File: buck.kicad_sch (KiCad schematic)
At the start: 0 parts

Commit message: Added Symbols and Buck Converter
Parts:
- added C1: 0.1uFCap, CAPC2012X94N, symbol group127:0.1uFCap
- added C2: 0.1uF, CAPC2012X94N, symbol group127:0.1uFCap
- added C3, C4: 22uF, CAPC2012X94N, symbol group127:0.1uFCap
- added L1: 6.8uH, 7447707068, symbol group127:Inductor
- added R1: 100k, RESC2012X60N, symbol group127:Resistor
- added R2: 13.7k, RESC2012X60N, symbol group127:Resistor
- added U1: LMR51430, Package_TO_SOT_SMD:SOT-23-6, symbol Regulator_Switching:LMR51430
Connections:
- new net: R1.1, R2.1, U1.4 (FB)
- new net: C3.1, C4.1, L1.2, R1.2
- new net: C2.1, U1.6 (CB)
- new net: C2.2, L1.1, U1.2 (SW)
- new net 15V: C1.2, U1.3 (VIN), U1.5 (EN)
- new net GND: C1.1, C3.2, C4.2, R2.2, U1.1 (GND)

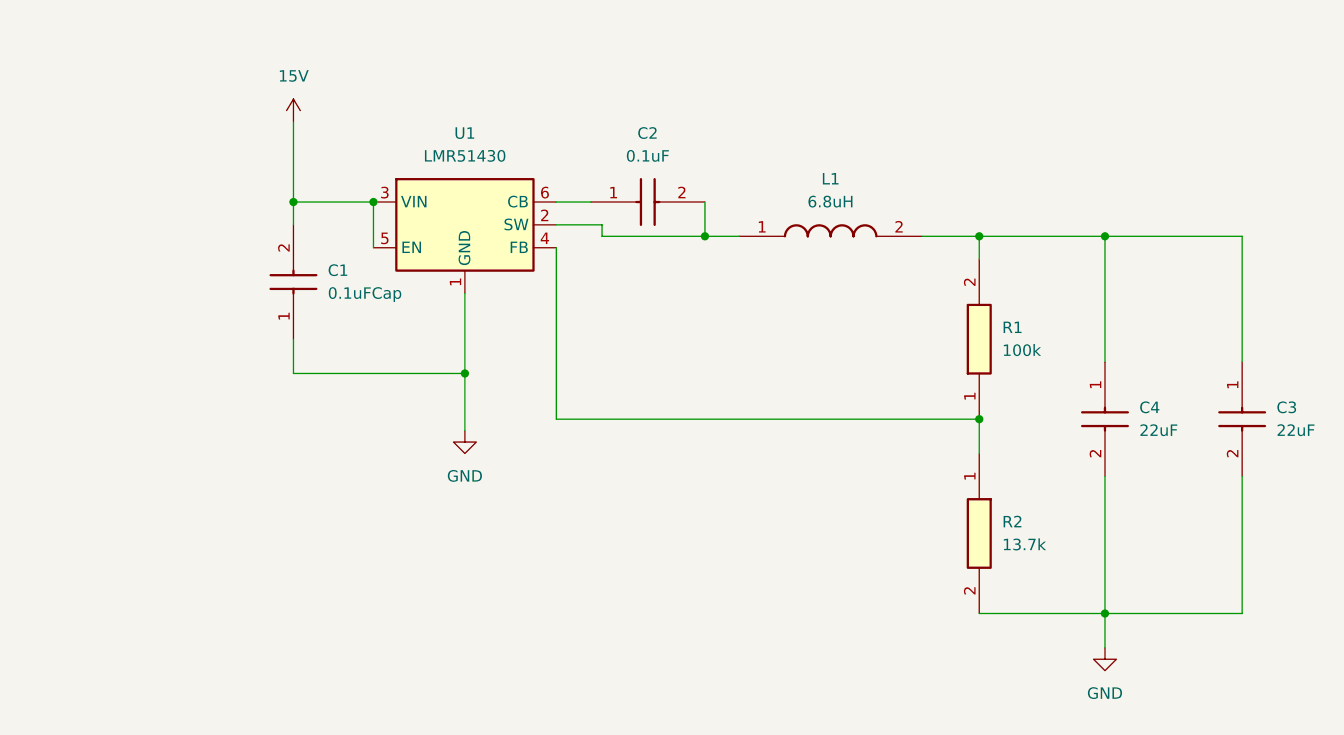
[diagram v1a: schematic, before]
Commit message: Update ldo.kicad_sch
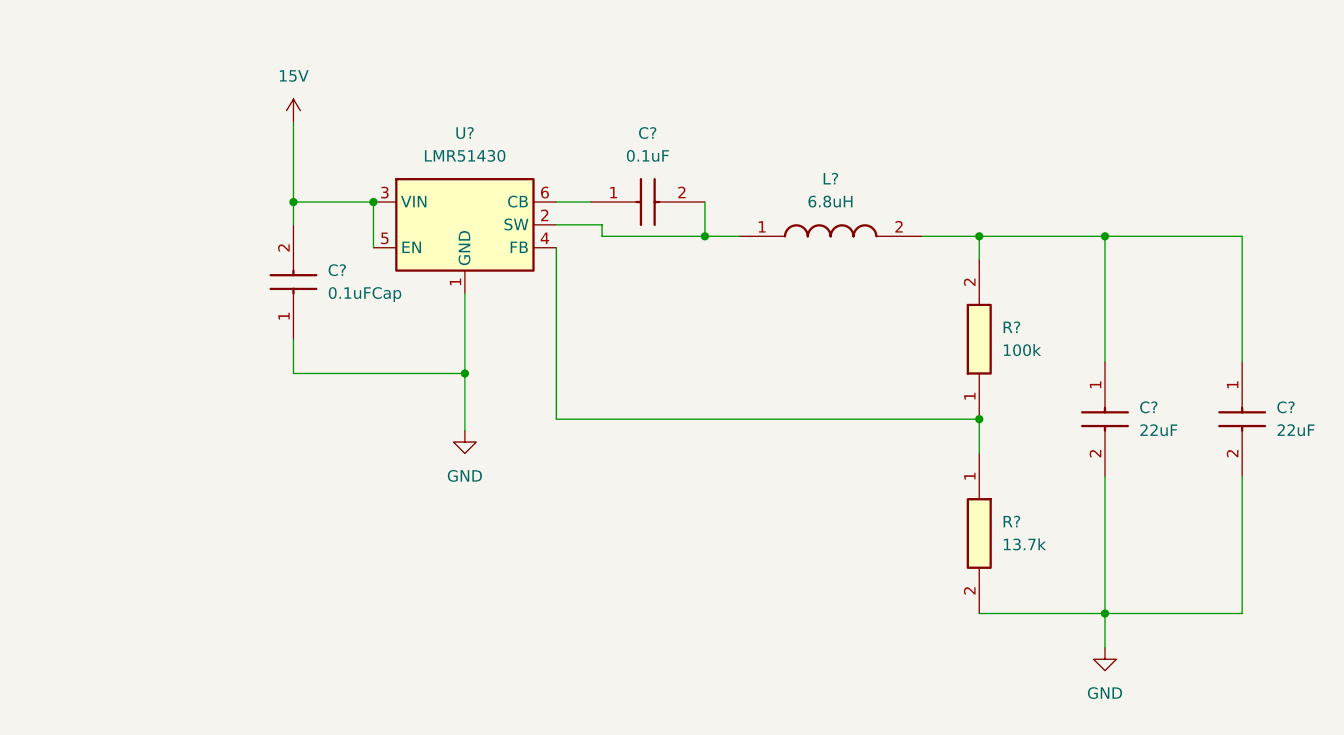
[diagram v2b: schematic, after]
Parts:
- renumbered C3 to C?, C2 to C?, C4 to C?, C1 to C?, L1 to L?, R1 to R?, R2 to R?, U1 to U?
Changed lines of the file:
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@@
 		(dnp no)
 		(fields_autoplaced yes)
-		(property "Reference" "R1"
+		(property "Reference" "R?"
 			(at 203.2 96.5199 90)
 			(effects
@@
 		)
 		(instances
+			(project "harm_drone"
+				(path "/5ce3566e-4e0f-420e-9b0d-3952cd3c63fd/9be4028a-d272-4251-aa6b-aa28299b7605"
+					(reference "R?")
+					(unit 1)
+				)
+			)
 			(project ""
 				(path "/973177bf-fda4-45db-b70f-878876a688dd"
@@
 		(dnp no)
 		(fields_autoplaced yes)
-		(property "Reference" "C3"
+		(property "Reference" "C?"
 			(at 233.68 105.4099 90)
 			(effects
@@
 		)
 		(instances
+			(project "harm_drone"
+				(path "/5ce3566e-4e0f-420e-9b0d-3952cd3c63fd/9be4028a-d272-4251-aa6b-aa28299b7605"
+					(reference "C?")
+					(unit 1)
+				)
+			)
 			(project "buck"
 				(path "/973177bf-fda4-45db-b70f-878876a688dd"
@@
 		(dnp no)
 		(fields_autoplaced yes)
-		(property "Reference" "#PWR02"
+		(property "Reference" "#PWR?"
 			(at 143.51 114.3 0)
 			(effects
@@
 		)
 		(instances
+			(project "harm_drone"
+				(path "/5ce3566e-4e0f-420e-9b0d-3952cd3c63fd/9be4028a-d272-4251-aa6b-aa28299b7605"
+					(reference "#PWR?")
+					(unit 1)
+				)
+			)
 			(project ""
 				(path "/973177bf-fda4-45db-b70f-878876a688dd"
@@
 		(dnp no)
 		(fields_autoplaced yes)
-		(property "Reference" "#PWR03"
+		(property "Reference" "#PWR?"
 			(at 214.63 138.43 0)
 			(effects
@@
 		)
 		(instances
+			(project "harm_drone"
+				(path "/5ce3566e-4e0f-420e-9b0d-3952cd3c63fd/9be4028a-d272-4251-aa6b-aa28299b7605"
+					(reference "#PWR?")
+					(unit 1)
+				)
+			)
 			(project "buck"
 				(path "/973177bf-fda4-45db-b70f-878876a688dd"
@@
 		(dnp no)
 		(fields_autoplaced yes)
-		(property "Reference" "C2"
+		(property "Reference" "C?"
 			(at 163.83 74.93 0)
 			(effects
@@
 		)
 		(instances
+			(project "harm_drone"
+				(path "/5ce3566e-4e0f-420e-9b0d-3952cd3c63fd/9be4028a-d272-4251-aa6b-aa28299b7605"
+					(reference "C?")
+					(unit 1)
+				)
+			)
 			(project "buck"
 				(path "/973177bf-fda4-45db-b70f-878876a688dd"
@@
 		(dnp no)
 		(fields_autoplaced yes)
-		(property "Reference" "L1"
+		(property "Reference" "L?"
 			(at 184.15 80.01 0)
 			(effects
@@
 		)
 		(instances
+			(project "harm_drone"
+				(path "/5ce3566e-4e0f-420e-9b0d-3952cd3c63fd/9be4028a-d272-4251-aa6b-aa28299b7605"
+					(reference "L?")
+					(unit 1)
+				)
+			)
 			(project ""
 				(path "/973177bf-fda4-45db-b70f-878876a688dd"
@@
 		(dnp no)
 		(fields_autoplaced yes)
-		(property "Reference" "#PWR01"
+		(property "Reference" "#PWR?"
 			(at 124.46 77.47 0)
 			(effects
@@
 		)
 		(instances
+			(project "harm_drone"
+				(path "/5ce3566e-4e0f-420e-9b0d-3952cd3c63fd/9be4028a-d272-4251-aa6b-aa28299b7605"
+					(reference "#PWR?")
+					(unit 1)
+				)
+			)
 			(project ""
 				(path "/973177bf-fda4-45db-b70f-878876a688dd"
@@
 		(dnp no)
 		(fields_autoplaced yes)
-		(property "Reference" "C4"
+		(property "Reference" "C?"
 			(at 218.44 105.4099 90)
 			(effects
@@
 		)
 		(instances
+			(project "harm_drone"
+				(path "/5ce3566e-4e0f-420e-9b0d-3952cd3c63fd/9be4028a-d272-4251-aa6b-aa28299b7605"
+					(reference "C?")
+					(unit 1)
+				)
+			)
 			(project "buck"
 				(path "/973177bf-fda4-45db-b70f-878876a688dd"
@@
 		(dnp no)
 		(fields_autoplaced yes)
-		(property "Reference" "U1"
+		(property "Reference" "U?"
 			(at 143.51 74.93 0)
 			(effects
@@
 		)
 		(instances
+			(project "harm_drone"
+				(path "/5ce3566e-4e0f-420e-9b0d-3952cd3c63fd/9be4028a-d272-4251-aa6b-aa28299b7605"
+					(reference "U?")
+					(unit 1)
+				)
+			)
 			(project ""
 				(path "/973177bf-fda4-45db-b70f-878876a688dd"
@@
 		(dnp no)
 		(fields_autoplaced yes)
-		(property "Reference" "C1"
+		(property "Reference" "C?"
 			(at 128.27 90.1699 90)
 			(effects
@@
 		)
 		(instances
+			(project "harm_drone"
+				(path "/5ce3566e-4e0f-420e-9b0d-3952cd3c63fd/9be4028a-d272-4251-aa6b-aa28299b7605"
+					(reference "C?")
+					(unit 1)
+				)
+			)
 			(project ""
 				(path "/973177bf-fda4-45db-b70f-878876a688dd"
@@
 		(dnp no)
 		(fields_autoplaced yes)
-		(property "Reference" "R2"
+		(property "Reference" "R?"
 			(at 203.2 118.1099 90)
 			(effects
@@
 		)
 		(instances
+			(project "harm_drone"
+				(path "/5ce3566e-4e0f-420e-9b0d-3952cd3c63fd/9be4028a-d272-4251-aa6b-aa28299b7605"
+					(reference "R?")
+					(unit 1)
+				)
+			)
 			(project ""
 				(path "/973177bf-fda4-45db-b70f-878876a688dd"

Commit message: standardize 5V and 3V3 labels
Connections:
- net 5V: now reaches C?.1, C?.1, L?.2, R?.2
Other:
- moved on the sheet: C?, L?, R?, U?

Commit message: finished up schematic
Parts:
- C10, C11, C8, C9: renamed from C?; footprint CAPC2012X94N -> Capacitor_SMD:C_0805_2012Metric
- L1: renamed from L?; footprint 7447707068 -> (none)
- R2, R3: renamed from R?; footprint RESC2012X60N -> Resistor_SMD:R_0805_2012Metric
- gave numbers to parts that had none: 1
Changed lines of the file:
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@@
 		(dnp no)
 		(fields_autoplaced yes)
-		(property "Reference" "R?"
+		(property "Reference" "R2"
 			(at 175.26 97.7899 90)
 			(effects
@@
 			)
 		)
-		(property "Footprint" "RESC2012X60N"
+		(property "Footprint" "Resistor_SMD:R_0805_2012Metric"
 			(at 268.91 93.98 0)
 			(effects
@@
 			(project "harm_drone"
 				(path "/5ce3566e-4e0f-420e-9b0d-3952cd3c63fd/9be4028a-d272-4251-aa6b-aa28299b7605"
-					(reference "R?")
+					(reference "R2")
 					(unit 1)
 				)
@@
 		(dnp no)
 		(fields_autoplaced yes)
-		(property "Reference" "C?"
+		(property "Reference" "C11"
 			(at 205.74 106.6799 90)
 			(effects
@@
 			)
 		)
-		(property "Footprint" "CAPC2012X94N"
+		(property "Footprint" "Capacitor_SMD:C_0805_2012Metric"
 			(at 105.74 110.49 0)
 			(effects
@@
 			(project "harm_drone"
 				(path "/5ce3566e-4e0f-420e-9b0d-3952cd3c63fd/9be4028a-d272-4251-aa6b-aa28299b7605"
-					(reference "C?")
+					(reference "C11")
 					(unit 1)
 				)
@@
 		(dnp no)
 		(fields_autoplaced yes)
-		(property "Reference" "#PWR?"
+		(property "Reference" "#PWR022"
 			(at 115.57 115.57 0)
 			(effects
@@
 			(project "harm_drone"
 				(path "/5ce3566e-4e0f-420e-9b0d-3952cd3c63fd/9be4028a-d272-4251-aa6b-aa28299b7605"
-					(reference "#PWR?")
+					(reference "#PWR022")
 					(unit 1)
 				)
@@
 		(dnp no)
 		(fields_autoplaced yes)
-		(property "Reference" "#PWR?"
+		(property "Reference" "#PWR023"
 			(at 186.69 139.7 0)
 			(effects
@@
 			(project "harm_drone"
 				(path "/5ce3566e-4e0f-420e-9b0d-3952cd3c63fd/9be4028a-d272-4251-aa6b-aa28299b7605"
-					(reference "#PWR?")
+					(reference "#PWR023")
 					(unit 1)
 				)
@@
 		(dnp no)
 		(fields_autoplaced yes)
-		(property "Reference" "C?"
+		(property "Reference" "C9"
 			(at 135.89 76.2 0)
 			(effects
@@
 			)
 		)
-		(property "Footprint" "CAPC2012X94N"
+		(property "Footprint" "Capacitor_SMD:C_0805_2012Metric"
 			(at 138.43 180.01 0)
 			(effects
@@
 			(project "harm_drone"
 				(path "/5ce3566e-4e0f-420e-9b0d-3952cd3c63fd/9be4028a-d272-4251-aa6b-aa28299b7605"
-					(reference "C?")
+					(reference "C9")
 					(unit 1)
 				)
@@
 		(dnp no)
 		(fields_autoplaced yes)
-		(property "Reference" "L?"
+		(property "Reference" "L1"
 			(at 156.21 81.28 0)
 			(effects
@@
 			)
 		)
-		(property "Footprint" "7447707068"
+		(property "Footprint" ""
 			(at 162.56 183.82 0)
 			(effects
@@
 			(project "harm_drone"
 				(path "/5ce3566e-4e0f-420e-9b0d-3952cd3c63fd/9be4028a-d272-4251-aa6b-aa28299b7605"
-					(reference "L?")
+					(reference "L1")
 					(unit 1)
 				)
@@
 		(dnp no)
 		(fields_autoplaced yes)
-		(property "Reference" "#PWR?"
+		(property "Reference" "#PWR021"
 			(at 96.52 78.74 0)
 			(effects
@@
 			(project "harm_drone"
 				(path "/5ce3566e-4e0f-420e-9b0d-3952cd3c63fd/9be4028a-d272-4251-aa6b-aa28299b7605"
-					(reference "#PWR?")
+					(reference "#PWR021")
 					(unit 1)
 				)
@@
 		(dnp no)
 		(fields_autoplaced yes)
-		(property "Reference" "C?"
+		(property "Reference" "C10"
 			(at 190.5 106.6799 90)
 			(effects
@@
 			)
 		)
-		(property "Footprint" "CAPC2012X94N"
+		(property "Footprint" "Capacitor_SMD:C_0805_2012Metric"
 			(at 90.5 110.49 0)
 			(effects
@@
 			(project "harm_drone"
 				(path "/5ce3566e-4e0f-420e-9b0d-3952cd3c63fd/9be4028a-d272-4251-aa6b-aa28299b7605"
-					(reference "C?")
+					(reference "C10")
 					(unit 1)
 				)
@@
 		(dnp no)
 		(fields_autoplaced yes)
-		(property "Reference" "U?"
+		(property "Reference" "U1"
 			(at 115.57 76.2 0)
 			(effects
@@
 			(project "harm_drone"
 				(path "/5ce3566e-4e0f-420e-9b0d-3952cd3c63fd/9be4028a-d272-4251-aa6b-aa28299b7605"
-					(reference "U?")
+					(reference "U1")
 					(unit 1)
 				)
@@
 		(dnp no)
 		(fields_autoplaced yes)
-		(property "Reference" "C?"
+		(property "Reference" "C8"
 			(at 100.33 91.4399 90)
 			(effects
@@
 			)
 		)
-		(property "Footprint" "CAPC2012X94N"
+		(property "Footprint" "Capacitor_SMD:C_0805_2012Metric"
 			(at 192.71 90.17 0)
 			(effects
@@
 			(project "harm_drone"
 				(path "/5ce3566e-4e0f-420e-9b0d-3952cd3c63fd/9be4028a-d272-4251-aa6b-aa28299b7605"
-					(reference "C?")
+					(reference "C8")
 					(unit 1)
 				)
@@
 		(dnp no)
 		(fields_autoplaced yes)
-		(property "Reference" "R?"
+		(property "Reference" "R3"
 			(at 175.26 119.3799 90)
 			(effects
@@
 			)
 		)
-		(property "Footprint" "RESC2012X60N"
+		(property "Footprint" "Resistor_SMD:R_0805_2012Metric"
 			(at 76.53 125.73 0)
 			(effects
@@
 			(project "harm_drone"
 				(path "/5ce3566e-4e0f-420e-9b0d-3952cd3c63fd/9be4028a-d272-4251-aa6b-aa28299b7605"
-					(reference "R?")
-					(unit 1)
-				)
+					(reference "R3")
+					(unit 1)
+				)

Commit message: initial PCB draft!
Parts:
- added J7: XT60-M, group127:XT60-M, symbol group127:XT60-M
- L1: footprint (none) -> group127:Inductor
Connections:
- net GND: now also J7.N (NEG)
- net 15V: no longer names the net of C8.2, U1.3 (VIN), U1.5 (EN)
- net 15V: now also J7.P (POS)
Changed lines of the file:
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@@
+	)
+	(symbol
+		(lib_id "group127:XT60-M")
+		(at 99.06 69.85 90)
+		(unit 1)
+		(exclude_from_sim no)
+		(in_bom yes)
+		(on_board yes)
+		(dnp no)
+		(fields_autoplaced yes)
+		(property "Reference" "J7"
+			(at 102.87 64.7699 90)
+			(effects
+				(font
+					(size 1.27 1.27)
+				)
+				(justify right)
+			)
+		)
+		(property "Value" "XT60-M"
+			(at 102.87 67.3099 90)
+			(effects
+				(font
+					(size 1.27 1.27)
+				)
+				(justify right)
+			)
+		)
+		(property "Footprint" "group127:XT60-M"
+			(at 99.06 69.85 0)
+			(effects
+				(font
+					(size 1.27 1.27)
+				)
+				(justify bottom)
+				(hide yes)
+			)
+		)
+		(property "Datasheet" ""
+			(at 99.06 69.85 0)
+			(effects
+				(font
+					(size 1.27 1.27)
+				)
+				(hide yes)
+			)
+		)
+		(property "Description" ""
+			(at 99.06 69.85 0)
+			(effects
+				(font
+					(size 1.27 1.27)
+				)
+				(hide yes)
+			)
+		)
+		(property "MF" "AMASS"
+			(at 99.06 69.85 0)
+			(effects
+				(font
+					(size 1.27 1.27)
+				)
+				(justify bottom)
+				(hide yes)
+			)
+		)
+		(property "MAXIMUM_PACKAGE_HEIGHT" "16.00 mm"
+			(at 99.06 69.85 0)
+			(effects
+				(font
+					(size 1.27 1.27)
+				)
+				(justify bottom)
+				(hide yes)
+			)
+		)
+		(property "Package" "Package"
+			(at 99.06 69.85 0)
+			(effects
+				(font
+					(size 1.27 1.27)
+				)
+				(justify bottom)
+				(hide yes)
+			)
+		)
+		(property "Price" "None"
+			(at 99.06 69.85 0)
+			(effects
+				(font
+					(size 1.27 1.27)
+				)
+				(justify bottom)
+				(hide yes)
+			)
+		)
+		(property "Check_prices" "https://www.snapeda.com/parts/XT60-M/AMASS/view-part/?ref=eda"
+			(at 99.06 69.85 0)
+			(effects
+				(font
+					(size 1.27 1.27)
+				)
+				(justify bottom)
+				(hide yes)
+			)
+		)
+		(property "STANDARD" "IPC 7351B"
+			(at 99.06 69.85 0)
+			(effects
+				(font
+					(size 1.27 1.27)
+				)
+				(justify bottom)
+				(hide yes)
+			)
+		)
+		(property "PARTREV" "V1.2"
+			(at 99.06 69.85 0)
+			(effects
+				(font
+					(size 1.27 1.27)
+				)
+				(justify bottom)
+				(hide yes)
+			)
+		)
+		(property "SnapEDA_Link" "https://www.snapeda.com/parts/XT60-M/AMASS/view-part/?ref=snap"
+			(at 99.06 69.85 0)
+			(effects
+				(font
+					(size 1.27 1.27)
+				)
+				(justify bottom)
+				(hide yes)
+			)
+		)
+		(property "MP" "XT60-M"
+			(at 99.06 69.85 0)
+			(effects
+				(font
+					(size 1.27 1.27)
+				)
+				(justify bottom)
+				(hide yes)
+			)
+		)
+		(property "Description_1" "\n                        \n                            Plug; DC supply; XT60; male; PIN: 2; for cable; soldered; 30A; 500V\n                        \n"
+			(at 99.06 69.85 0)
+			(effects
+				(font
+					(size 1.27 1.27)
+				)
+				(justify bottom)
+				(hide yes)
+			)
+		)
+		(property "Availability" "Not in stock"
+			(at 99.06 69.85 0)
+			(effects
+				(font
+					(size 1.27 1.27)
+				)
+				(justify bottom)
+				(hide yes)
+			)
+		)
+		(property "MANUFACTURER" "AMASS"
+			(at 99.06 69.85 0)
+			(effects
+				(font
+					(size 1.27 1.27)
+				)
+				(justify bottom)
+				(hide yes)
+			)
+		)
+		(pin "P"
+		)
+		(pin "N"
+		)
+		(instances
+			(project ""
+				(path "/5ce3566e-4e0f-420e-9b0d-3952cd3c63fd/9be4028a-d272-4251-aa6b-aa28299b7605"
+					(reference "J7")
+					(unit 1)
+				)
+			)
+		)
 	)
 	(symbol
@@
 			)
 		)
-		(property "Footprint" ""
+		(property "Footprint" "group127:Inductor"
 			(at 162.56 183.82 0)
 			(effects
@@
 				(path "/973177bf-fda4-45db-b70f-878876a688dd"
 					(reference "L1")
-					(unit 1)
-				)
-			)
-		)
-	)
-	(symbol
-		(lib_id "power:VCC")
-		(at 96.52 74.93 0)
-		(unit 1)
-		(exclude_from_sim no)
-		(in_bom yes)
-		(on_board yes)
-		(dnp no)
-		(fields_autoplaced yes)
-		(property "Reference" "#PWR021"
-			(at 96.52 78.74 0)
-			(effects
-				(font
-					(size 1.27 1.27)
-				)
-				(hide yes)
-			)
-		)
-		(property "Value" "15V"
-			(at 96.52 69.85 0)
-			(effects
-				(font
-					(size 1.27 1.27)
-				)
-			)
-		)
-		(property "Footprint" ""
-			(at 96.52 74.93 0)
-			(effects
-				(font
-					(size 1.27 1.27)
-				)
-				(hide yes)
-			)
-		)
-		(property "Datasheet" ""
-			(at 96.52 74.93 0)
-			(effects
-				(font
-					(size 1.27 1.27)
-				)
-				(hide yes)
-			)
-		)
-		(property "Description" "Power symbol creates a global label with name \"VCC\""
-			(at 96.52 74.93 0)
-			(effects
-				(font
-					(size 1.27 1.27)
-				)
-				(hide yes)
-			)
-		)
-		(pin "1"
-		)
-		(instances
-			(project "harm_drone"
-				(path "/5ce3566e-4e0f-420e-9b0d-3952cd3c63fd/9be4028a-d272-4251-aa6b-aa28299b7605"
-					(reference "#PWR021")
-					(unit 1)
-				)
-			)
-			(project ""
-				(path "/973177bf-fda4-45db-b70f-878876a688dd"
-					(reference "#PWR01")
 					(unit 1)
 				)
@@
 					(unit 1)
 				)
+			)
+		)
+	)
+	(symbol
+		(lib_id "power:GND")
+		(at 99.06 74.93 0)
+		(unit 1)
+		(exclude_from_sim no)
+		(in_bom yes)
+		(on_board yes)
+		(dnp no)
+		(fields_autoplaced yes)
+		(property "Reference" "#PWR019"
+			(at 99.06 81.28 0)
+			(effects
+				(font
+					(size 1.27 1.27)
+				)
+				(hide yes)
+			)
+		)
+		(property "Value" "GND"
+			(at 99.06 80.01 0)
+			(effects
+				(font
+					(size 1.27 1.27)
+				)
+			)
+		)
+		(property "Footprint" ""
+			(at 99.06 74.93 0)
+			(effects
+				(font
+					(size 1.27 1.27)
+				)
+				(hide yes)
+			)
+		)
+		(property "Datasheet" ""
+			(at 99.06 74.93 0)
+			(effects
+				(font
+					(size 1.27 1.27)
+				)
+				(hide yes)
+			)
+		)
+		(property "Description" "Power symbol creates a global label with name \"GND\" , ground"
+			(at 99.06 74.93 0)
+			(effects
+				(font
+					(size 1.27 1.27)
+				)
+				(hide yes)
+			)
+		)
+		(pin "1"
+		)
+		(instances
+			(project "harm_drone"
+				(path "/5ce3566e-4e0f-420e-9b0d-3952cd3c63fd/9be4028a-d272-4251-aa6b-aa28299b7605"
+					(reference "#PWR019")
+					(unit 1)
+				)

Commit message: before differential routing
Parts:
- C8: value 0.1uFCap -> 0.1uF
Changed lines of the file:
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@@
 			)
 		)
-		(property "Value" "0.1uFCap"
+		(property "Value" "0.1uF"
 			(at 100.33 93.9799 90)
 			(effects
